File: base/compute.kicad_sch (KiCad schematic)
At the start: 49 parts, among them IC4 DMP6023LSS-13, J1 USB_C_Receptacle_USB2.0_16P, J3 2-84952-0, J4 power, U1 MCP1700T-1202ETT, U3 LD1117S33TR_SOT223, U6 MCP1700T-2802E, U7 USBLC6-2SC6, U8 AP63205WU-7, U9 AP63203WU-7

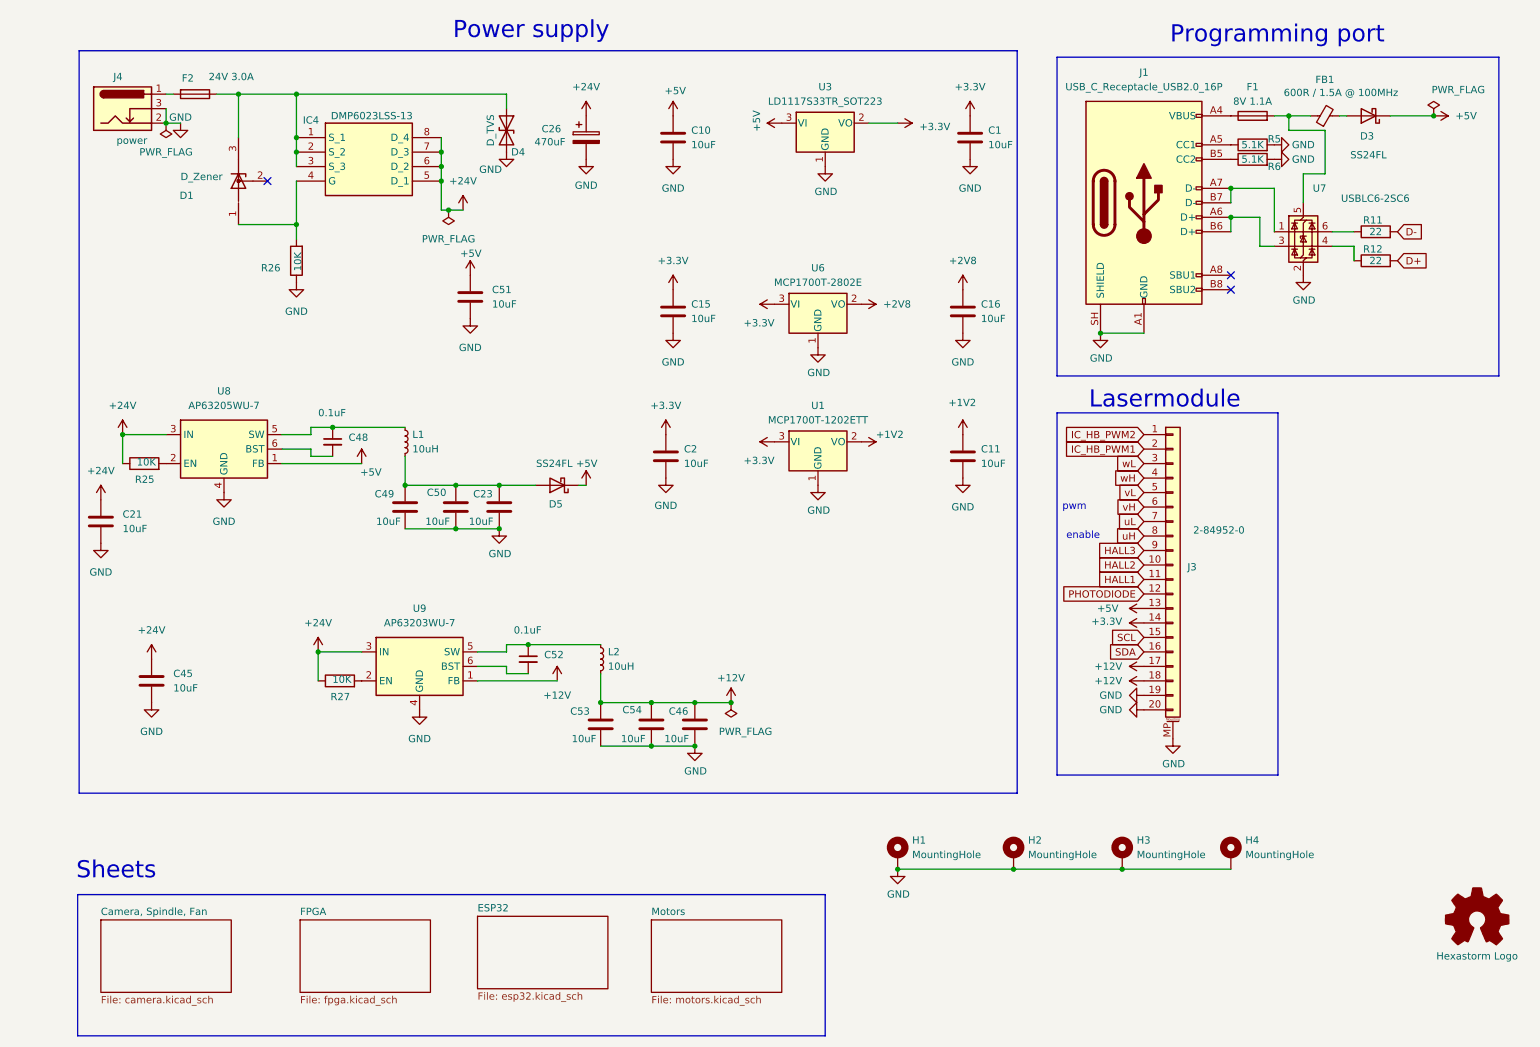
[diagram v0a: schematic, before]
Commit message: improved powernet, fixed bugs, tuned tracks for camera
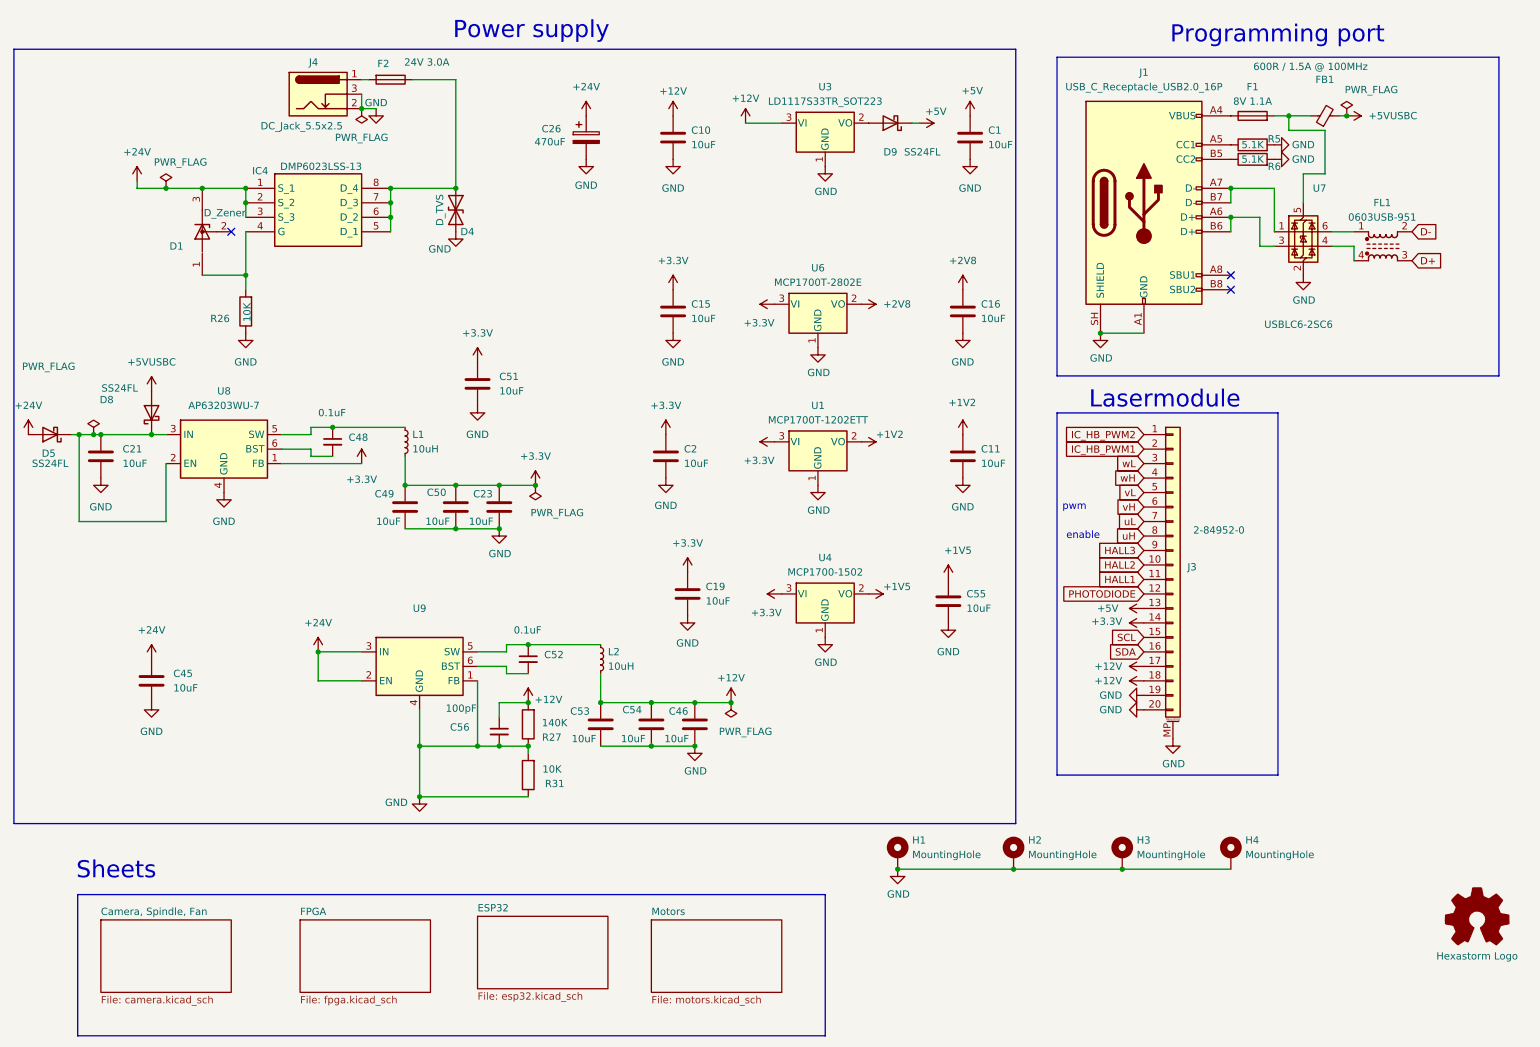
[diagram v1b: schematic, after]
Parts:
- removed D3: SS24FL, Diode_SMD:D_SMA, symbol Diode:SS24
- removed R11, R12: 22, Resistor_SMD:R_0805_2012Metric, symbol Device:R
- removed R25: 10K, Resistor_SMD:R_0805_2012Metric, symbol Device:R
- added C19, C55: 10uF, Capacitor_SMD:C_0805_2012Metric_Pad1.18x1.45mm_HandSolder, symbol Device:C
- added C56: 100pF, Capacitor_SMD:C_0805_2012Metric_Pad1.18x1.45mm_HandSolder, symbol Device:C_Small
- added D8, D9: SS24FL, Diode_SMD:D_SMA, symbol Diode:SS24
- added FL1: 0603USB-951, Inductor_SMD:L_CommonModeChoke_Coilcraft_0603USB, symbol Filter:0603USB-951
- added R31: 10K, Resistor_SMD:R_0805_2012Metric, symbol Device:R
- added U4: MCP1700-1502, Package_TO_SOT_SMD:SOT-23, symbol Regulator_Linear:MCP1700x-120xxTT
- D4: farnell# 2765106 -> 1827683; manf# SMBJ13CA -> SMBJ26CA; mouser# 652-SMBJ13CA -> 652-SMBJ26CA
- J4: value power -> DC_Jack_5.5x2.5; farnell# 4814431 -> 4814432; manf# PJ-036AH-SMT-TR -> PJ-036BH-SMT-TR; mouser# 490-PJ-036AH-SMT-TR -> 490-PJ-036BH-SMT-TR
- R27: value 10K -> 140K; farnell# 2826162 -> 3951210; manf# CRCW080510K0JNEAC -> RC0805FR-07140KL; mouser# 71-CRCW080510K0JNEAC -> 603-RC0805FR-07140KL
- U3: farnell# 1467779 -> 3007506; manf# LD1117S33CTR -> LM1117MPX-5.0/NOPB; mouser# 511-LD1117S33C -> 926-LM1117MPX5.0NOPB
- U8: value AP63205WU-7 -> AP63203WU-7; farnell# 3518308 -> 3518307; manf# AP63205WU-7 -> AP63203WU-7; mouser# 621-AP63205WU-7 -> 621-AP63203WU-7
- U9: value AP63203WU-7 -> (none); farnell# 3518307 -> 3518305; manf# AP63203WU-7 -> AP63200WU-7; mouser# 621-AP63203WU-7 -> 621-AP63200WU-7
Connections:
- net +12V: now also C10.1, R27.2, U3.3 (VI), C56.1; no longer U9.1 (FB)
- net +24V: now also D1.3 (K), D5.2 (A), IC4.1 (S_1), IC4.2 (S_2), IC4.3 (S_3), U9.2 (EN); no longer C21.1, IC4.5 (D_1), IC4.6 (D_2), IC4.7 (D_3), IC4.8 (D_4), R27.1, U8.3 (IN)
- net +3.3V: now also C23.1, C49.1, C50.1, C51.1, L1.2, U8.1 (FB), C19.1, U4.3 (VI); no longer C1.1, U3.2 (VO)
- net +5V: now also C1.1, D9.1 (K); no longer C10.1, C51.1, D5.1 (K), U3.3 (VI), U8.1 (FB)
- net D+: now also FL1.3
- net D-: now also FL1.2
- net GND: now also R27.1, U9.1 (FB), C19.2, C55.2, C56.2, R31.1, R31.2, U4.1 (GND)
- net at U7.4 (I/O2): now also FL1.4
- net at U7.6 (I/O1): now also FL1.1
- net +5VUSBC: now reaches FB1.2
- net +5VUSBC: now also D8.2 (A)
- net at U8.2 (EN): now also C21.1, D5.1 (K), U8.3 (IN), D8.1 (K)
- new net: D4.1 (A1), F2.1, IC4.5 (D_1), IC4.6 (D_2), IC4.7 (D_3), IC4.8 (D_4)
- new net: D9.2 (A), U3.2 (VO)
- new net +1V5: C55.1, U4.2 (VO)
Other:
- moved on the sheet: C21, C51, D1, D4, D5, F2, IC4, J4, R26

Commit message: send to fab
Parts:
- removed D9: SS24FL, Diode_SMD:D_SMA, symbol Diode:SS24
- D1: farnell# 637-BZX84C12 -> 2675184; mouser# 2675184 -> 863-BZX84C12LT1G
- FL1: footprint Inductor_SMD:L_CommonModeChoke_Coilcraft_0603USB -> footprints:L_CommonModeChoke_Coilcraft_0603USB; mouser# 994-0603USB-951MLC -> 994-0603USB-142MLC
- H1, H2, H3, H4: footprint MountingHole:MountingHole_2.2mm_M2_Pad_Via -> MountingHole:MountingHole_2.5mm_Pad_Via
- L1, L2: mouser# 652-SRP5030T-100M -> 810-SPM5030T-100M-HZ
- R26, R31: value 10K -> 5.1K; farnell# 2826162 -> 1469937; manf# CRCW080510K0JNEAC -> CRCW08055K10FKEA; mouser# 71-CRCW080510K0JNEAC -> -71-CRCW0805-5.1K-E3
- R27: value 140K -> 71.5K; farnell# 3951210 -> 3952038; manf# RC0805FR-07140KL -> RC0805FR-0771K5L; mouser# 603-RC0805FR-07140KL -> 603-RC0805FR-0771K5L
- R5, R6: mouser# 71-CRCW0805-5.1K-E3 -> -71-CRCW0805-5.1K-E3
- U3: value LD1117S33TR_SOT223 -> LM1117MPX-5.0/NOPB; footprint Package_TO_SOT_SMD:SOT-23 -> Package_TO_SOT_SMD:SOT-223-3_TabPin2; symbol Regulator_Linear:MCP1700x-330xxTT -> Regulator_Linear:LD1117S50TR_SOT223
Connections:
- net +5V: now also U3.2 (VO)
- net GND: no longer C56.2, R27.1, R31.2, U9.1 (FB)
- new net: C56.2, R27.1, R31.2, U9.1 (FB)
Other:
- note added: "do not mix with 5V"
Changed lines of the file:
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@@
 		)
 	)
+	(text "do not mix with 5V"
+		(exclude_from_sim no)
+		(at 260.858 36.068 0)
+		(effects
+			(font
+				(size 1.27 1.27)
+			)
+		)
+	)
 	(junction
 		(at 31.75 87.63)
@@
 	)
 	(junction
-		(at 88.9 142.24)
-		(diameter 0)
-		(color 0 0 0 0)
-	)
-	(junction
 		(at 86.36 96.52)
 		(diameter 0)
@@
 	)
 	(junction
-		(at 99.06 142.24)
-		(diameter 0)
-		(color 0 0 0 0)
-	)
-	(junction
 		(at 241.3 31.75)
 		(diameter 0)
@@
 	(wire
 		(pts
-			(xy 175.26 33.02) (xy 176.53 33.02)
-		)
-		(stroke
-			(width 0)
-			(type default)
-		)
-	)
-	(wire
-		(pts
 			(xy 231.14 49.53) (xy 236.22 49.53)
 		)
@@
 	(wire
 		(pts
-			(xy 99.06 142.24) (xy 88.9 142.24)
-		)
-		(stroke
-			(width 0)
-			(type default)
-		)
-	)
-	(wire
-		(pts
 			(xy 29.21 87.63) (xy 29.21 102.87)
 		)
@@
 	(wire
 		(pts
-			(xy 88.9 142.24) (xy 88.9 151.13)
-		)
-		(stroke
-			(width 0)
-			(type default)
-		)
-	)
-	(wire
-		(pts
 			(xy 78.74 30.48) (xy 78.74 27.94)
 		)
@@
 	(wire
 		(pts
-			(xy 88.9 135.89) (xy 88.9 142.24)
+			(xy 88.9 135.89) (xy 88.9 151.13)
 		)
 		(stroke
@@
 			)
 		)
-		(property "Footprint" "MountingHole:MountingHole_2.2mm_M2_Pad_Via"
+		(property "Footprint" "MountingHole:MountingHole_2.5mm_Pad_Via"
 			(at 193.04 161.29 0)
 			(hide yes)
@@
 		(dnp no)
 		(property "Reference" "R5"
-			(at 238.76 35.814 90)
+			(at 234.95 34.29 90)
 			(show_name no)
 			(do_not_autoplace no)
@@
 			)
 		)
-		(property "mouser#" "71-CRCW0805-5.1K-E3"
+		(property "mouser#" "-71-CRCW0805-5.1K-E3"
 			(at 234.95 36.83 90)
 			(hide yes)
@@
 			)
 		)
-		(property "Value" "10K"
+		(property "Value" "5.1K"
 			(at 113.792 146.304 0)
 			(show_name no)
@@
 			)
 		)
-		(property "farnell#" "2826162"
+		(property "farnell#" "1469937"
 			(at 107.95 147.32 0)
 			(hide yes)
@@
 			)
 		)
-		(property "manf#" "CRCW080510K0JNEAC"
+		(property "manf#" "CRCW08055K10FKEA"
 			(at 107.95 147.32 0)
 			(hide yes)
@@
 			)
 		)
-		(property "mouser#" "71-CRCW080510K0JNEAC"
+		(property "mouser#" "-71-CRCW0805-5.1K-E3"
 			(at 107.95 147.32 0)
 			(hide yes)
@@
 			)
 		)
-		(property "mouser#" "652-SRP5030T-100M"
+		(property "mouser#" "810-SPM5030T-100M-HZ"
 			(at 86.36 88.9 0)
 			(hide yes)
@@
 			)
 		)
-		(property "Footprint" "MountingHole:MountingHole_2.2mm_M2_Pad_Via"
+		(property "Footprint" "MountingHole:MountingHole_2.5mm_Pad_Via"
 			(at 212.09 161.29 0)
 			(hide yes)
@@
 			)
 		)
-		(property "mouser#" "2675184"
+		(property "mouser#" "863-BZX84C12LT1G "
 			(at 50.8 52.07 90)
 			(hide yes)
@@
 			)
 		)
-		(property "farnell#" "637-BZX84C12"
+		(property "farnell#" "2675184"
 			(at 50.8 52.07 90)
 			(hide yes)
@@
 			)
 		)
-		(property "Footprint" "MountingHole:MountingHole_2.2mm_M2_Pad_Via"
+		(property "Footprint" "MountingHole:MountingHole_2.5mm_Pad_Via"
 			(at 172.72 161.29 0)
 			(hide yes)
@@
 		(dnp no)
 		(property "Reference" "R6"
-			(at 238.76 40.64 90)
+			(at 234.95 41.91 90)
 			(show_name no)
 			(do_not_autoplace no)
@@
 			)
 		)
-		(property "mouser#" "71-CRCW0805-5.1K-E3"
+		(property "mouser#" "-71-CRCW0805-5.1K-E3"
 			(at 234.95 39.37 90)
 			(hide yes)
@@
 			)
 		)
-		(property "Value" "10K"
-			(at 58.674 64.516 90)
+		(property "Value" "5.1K"
+			(at 64.77 67.31 0)
 			(show_name no)
 			(do_not_autoplace no)
@@
 			)
 		)
-		(property "farnell#" "2826162"
+		(property "farnell#" "1469937"
 			(at 58.42 66.04 0)
 			(hide yes)
@@
 			)
 		)
-		(property "manf#" "CRCW080510K0JNEAC"
+		(property "manf#" "CRCW08055K10FKEA"
 			(at 58.42 66.04 0)
 			(hide yes)
@@
 			)
 		)
-		(property "mouser#" "71-CRCW080510K0JNEAC"
+		(property "mouser#" "-71-CRCW0805-5.1K-E3"
 			(at 58.42 66.04 0)
 			(hide yes)
@@
 			)
 		)
-		(property "mouser#" "652-SRP5030T-100M"
+		(property "mouser#" "810-SPM5030T-100M-HZ"
 			(at 120.65 127 0)
 			(hide yes)
@@
 	)
 	(symbol
-		(lib_id "Regulator_Linear:MCP1700x-330xxTT")
+		(lib_id "Regulator_Linear:LD1117S50TR_SOT223")
 		(at 160.02 33.02 0)
 		(unit 1)
@@
 			)
 		)
-		(property "Value" "LD1117S33TR_SOT223"
+		(property "Value" "LM1117MPX-5.0/NOPB"
 			(at 160.02 29.21 0)
 			(show_name no)
@@
 			)
 		)
-		(property "Footprint" "Package_TO_SOT_SMD:SOT-23"
-			(at 160.02 27.305 0)
+		(property "Footprint" "Package_TO_SOT_SMD:SOT-223-3_TabPin2"
+			(at 160.02 27.94 0)
 			(hide yes)
 			(show_name no)
@@
 			)
 		)
-		(property "Datasheet" "http://ww1.microchip.com/downloads/en/DeviceDoc/20001826D.pdf"
-			(at 160.02 33.02 0)
+		(property "Datasheet" "http://www.st.com/st-web-ui/static/active/en/resource/technical/document/datasheet/CD00000544.pdf"
+			(at 162.56 39.37 0)
 			(hide yes)
 			(show_name no)
@@
 			)
 		)
-		(property "Description" "250mA Low Quiscent Current LDO, 3.3V output, SOT-23"
+		(property "Description" "800mA Fixed Low Drop Positive Voltage Regulator, Fixed Output 5.0V, SOT-223"
 			(at 160.02 33.02 0)
 			(hide yes)
@@
 	(symbol
 		(lib_id "power:+5V")
-		(at 176.53 33.02 270)
+		(at 167.64 33.02 270)
 		(unit 1)
 		(body_style 1)
@@
 		(dnp no)
 		(property "Reference" "#PWR0127"
-			(at 172.72 33.02 0)
+			(at 163.83 33.02 0)
 			(hide yes)
 			(show_name no)
@@
 		)
 		(property "Value" "+5V"
-			(at 177.546 30.988 90)
+			(at 168.656 30.988 90)
 			(show_name no)
 			(do_not_autoplace no)
@@
 		)
 		(property "Footprint" ""
-			(at 176.53 33.02 0)
+			(at 167.64 33.02 0)
 			(hide yes)
 			(show_name no)
@@
 		)
 		(property "Datasheet" ""
-			(at 176.53 33.02 0)
+			(at 167.64 33.02 0)
 			(hide yes)
 			(show_name no)
@@
 		)
 		(property "Description" "Power symbol creates a global label with name \"+5V\""
-			(at 176.53 33.02 0)
+			(at 167.64 33.02 0)
 			(hide yes)
 			(show_name no)
@@
 	)
 	(symbol
-		(lib_id "Diode:SS24")
-		(at 171.45 33.02 180)
-		(unit 1)
-		(body_style 1)
-		(exclude_from_sim no)
-		(in_bom yes)
-		(on_board yes)
-		(in_pos_files yes)
-		(dnp no)
-		(property "Reference" "D9"
-			(at 171.45 38.1 0)
-			(show_name no)
-			(do_not_autoplace no)
-			(effects
-				(font
-					(size 1.27 1.27)
-				)
-			)
-		)
-		(property "Value" "SS24FL"
-			(at 177.038 38.1 0)
-			(show_name no)
-			(do_not_autoplace no)
-			(effects
-				(font
-					(size 1.27 1.27)
-				)
-			)
-		)
-		(property "Footprint" "Diode_SMD:D_SMA"
-			(at 171.45 28.575 0)
-			(hide yes)
-			(show_name no)
-			(do_not_autoplace no)
-			(effects
-				(font
-					(size 1.27 1.27)
-				)
-			)
-		)
-		(property "Datasheet" "https://www.vishay.com/docs/88748/ss22.pdf"
-			(at 171.45 33.02 0)
-			(hide yes)
-			(show_name no)
-			(do_not_autoplace no)
-			(effects
-				(font
-					(size 1.27 1.27)
-				)
-			)
-		)
-		(property "Description" "40V 2A Schottky Diode, SMA"
-			(at 171.45 33.02 0)
-			(hide yes)
-			(show_name no)
-			(do_not_autoplace no)
-			(effects
-				(font
-					(size 1.27 1.27)
-				)
-			)
-		)
-		(property "OLDFootprint" ""
-			(at 171.45 33.02 0)
-			(hide yes)
-			(show_name no)
-			(do_not_autoplace no)
-			(effects
-				(font
-					(size 1.27 1.27)
-				)
-			)
-		)
-		(property "farnell#" "2822566"
-			(at 171.45 33.02 0)
-			(hide yes)
-			(show_name no)
-			(do_not_autoplace no)
-			(effects
-				(font
-					(size 1.27 1.27)
-				)
-			)
-		)
-		(property "manf#" "SS24FL"
-			(at 171.45 33.02 0)
-			(hide yes)
-			(show_name no)
-			(do_not_autoplace no)
-			(effects
-				(font
-					(size 1.27 1.27)
-				)
-			)
-		)
-		(property "mouser#" "512-SS24FL"
-			(at 171.45 33.02 0)
-			(hide yes)
-			(show_name no)
-			(do_not_autoplace no)
-			(effects
-				(font
-					(size 1.27 1.27)
-				)
-			)
-		)
-		(pin "1"
-		)
-		(pin "2"
-		)
-		(instances
-			(project "compute"
-				(path "/3f5fe6b7-98fc-4d3e-9567-f9f7202d1455"
-					(reference "D9")
-					(unit 1)
-				)
-			)
-		)
-	)
-	(symbol
 		(lib_id "power:GND")
 		(at 215.9 133.35 270)
@@
 			)
 		)
-		(property "Value" "140K"
+		(property "Value" "71.5K"
 			(at 114.808 138.176 0)
 			(show_name no)
@@
 			)
 		)
-		(property "farnell#" "3951210"
+		(property "farnell#" "3952038"
 			(at 107.95 138.43 0)
 			(hide yes)
@@
 			)
 		)
-		(property "manf#" "RC0805FR-07140KL"
+		(property "manf#" "RC0805FR-0771K5L"
 			(at 107.95 138.43 0)
 			(hide yes)
@@
 			)
 		)
-		(property "mouser#" "603-RC0805FR-07140KL "
+		(property "mouser#" "603-RC0805FR-0771K5L"
 			(at 107.95 138.43 0)
 			(hide yes)
@@
 			)
 		)
-		(property "Footprint" "Inductor_SMD:L_CommonModeChoke_Coilcraft_0603USB"
+		(property "Footprint" "footprints:L_CommonModeChoke_Coilcraft_0603USB"
 			(at 257.81 60.96 0)
 			(hide yes)
@@
 			)
 		)
-		(property "mouser#" "994-0603USB-951MLC"
+		(property "mouser#" "994-0603USB-142MLC"
 			(at 257.81 54.61 0)
 			(hide yes)
@@
 			)
 		)
-		(property "Footprint" "MountingHole:MountingHole_2.2mm_M2_Pad_Via"
+		(property "Footprint" "MountingHole:MountingHole_2.5mm_Pad_Via"
 			(at 231.14 161.29 0)
 			(hide yes)
